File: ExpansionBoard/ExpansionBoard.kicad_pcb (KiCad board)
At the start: 2 copper layers, 90 x 80 mm, 11 parts, among them J2 Screw_Terminal_01x02, J3 Conn_02x19_Odd_Even, J4 Conn_02x19_Odd_Even

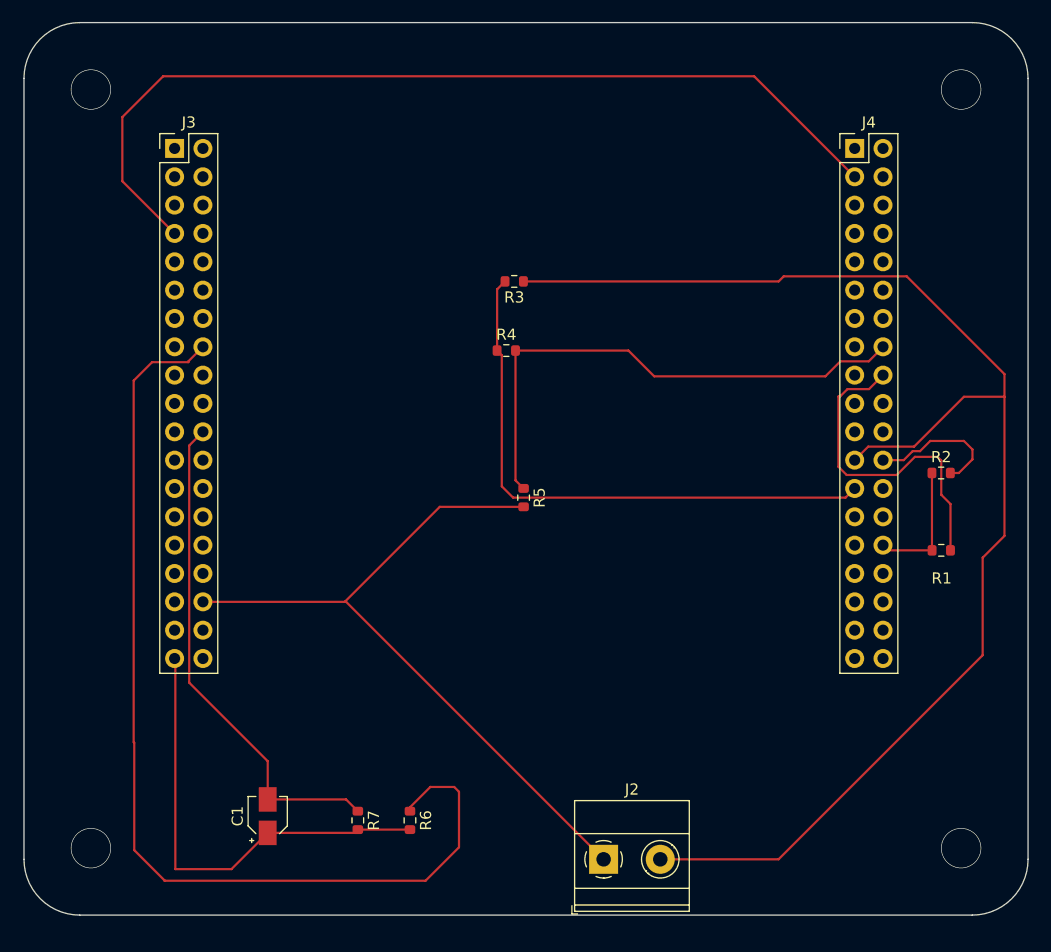
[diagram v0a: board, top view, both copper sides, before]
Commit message: Revision PCB e Intento ADCs
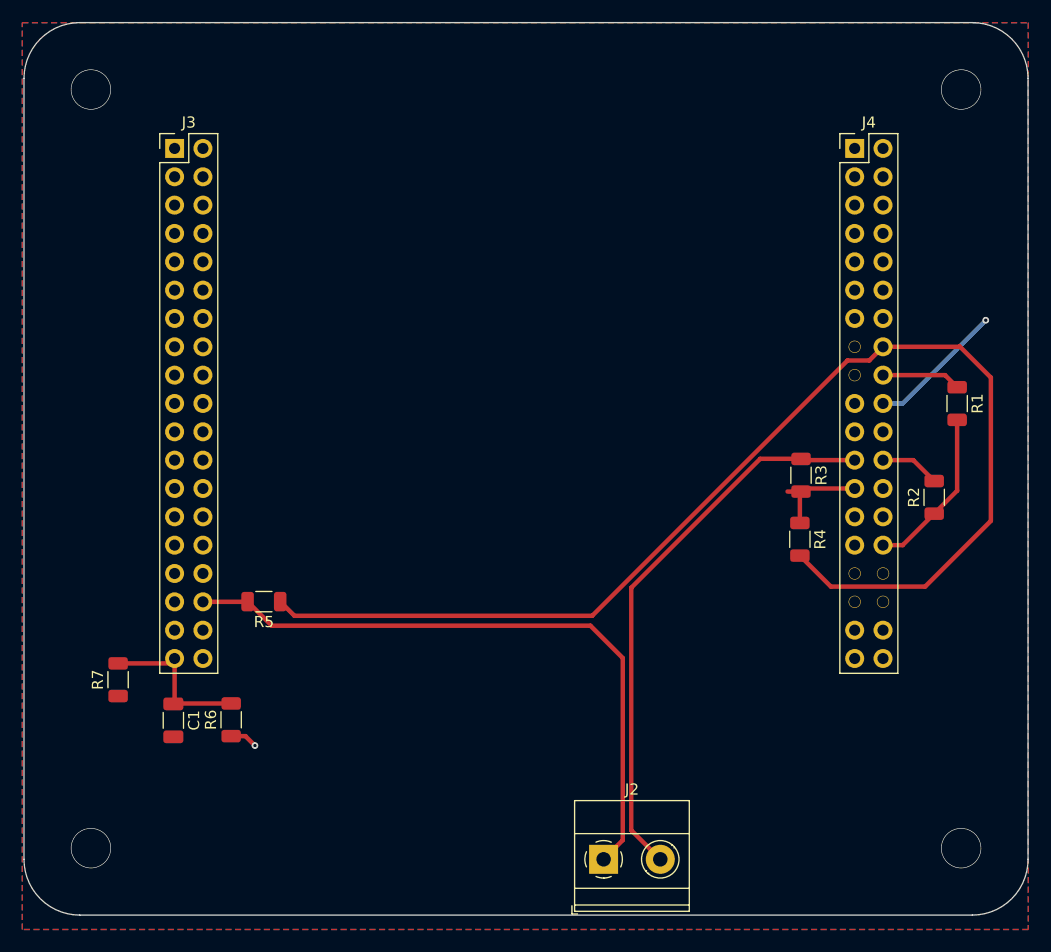
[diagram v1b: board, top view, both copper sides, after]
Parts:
- C1: footprint Capacitor_SMD:CP_Elec_3x5.3 -> Capacitor_SMD:C_1206_3216Metric
- R1, R2, R3, R4, R5, R6, R7: footprint Resistor_SMD:R_0603_1608Metric -> Resistor_SMD:R_1206_3216Metric
- moved R4 31.3 mm to (139.5, 126.3), turned to -90 degrees
- moved R3 31.0 mm to (139.6, 120.6), turned to -90 degrees
- moved R5 25.1 mm to (91.5, 131.9), turned to 180 degrees
- moved R7 24.9 mm to (78.4, 138.9), turned to 90 degrees
- moved R6 18.4 mm to (88.6, 142.5), turned to 90 degrees
- moved R1 13.2 mm to (153.6, 114.1), turned to -90 degrees
- moved C1 12.1 mm to (83.4, 142.5), turned to -90 degrees
- moved R2 2.27 mm to (151.6, 122.6), turned to 90 degrees
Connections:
- J4 pad 3: PB8 -> unconnected-(J4-Pin_3-Pad3)
- J4 pad 34: PC4 -> unconnected-(J4-Pin_34-Pad34)
- J4 pad 37: PC5 -> unconnected-(J4-Pin_37-Pad37)
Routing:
- net 3V3: track 91.8 -> 2.49 mm, vias 0 -> 1
- net PB8: track 83.3 -> 0.00 mm
- net PA8: track 125.2 -> 50.3 mm
- net PB12: track 47.7 -> 109.1 mm
- net PB10: track 51.2 -> 8.99 mm
- net GND: track 44.9 -> 12.3 mm, vias 0 -> 1
- net PC3: track 41.4 -> 14.7 mm
- net PB11: track 29.8 -> 7.09 mm
- net PB1: track 12.4 -> 5.36 mm
- net PB0: track 65.0 -> 58.5 mm
- net PB13: track 11.5 -> 16.3 mm
- added copper zone on B.Cu, net 3V3
- added copper zone on F.Cu, net GND

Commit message: TFG Finalizado V1
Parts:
- added G***: LOGO, etsii:ETSII512, F.Cu at (114.8, 94.0)
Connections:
- J4 pad 18: PB11 -> PA0
- J4 pad 24: PB1 -> PA6
- R1 pad 1: PB11 -> PA0
- R2 pad 2: PB1 -> PA6
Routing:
- net PA0: track 0.00 -> 74.6 mm
- net PA6: track 0.00 -> 39.8 mm, vias 0 -> 1
- net PB11: track 7.09 -> 0.00 mm
- net PB1: track 5.36 -> 0.00 mm
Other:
- board text added: "Emilio Silvestre Salvador Melendez"
